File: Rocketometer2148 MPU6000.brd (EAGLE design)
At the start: 55.9 x 22.9 mm, 70 parts, among them J001 USB_MICROB_JST, J301 JST 2mm, J401 M06, J402 M06, J701 MICROSD-SOCKET, Q050 PMOS, U101 BMP180, U201 5319, U301 73831, U401 LPC2148, U601 MPU6000, U801 HMC5883L, U902 ADXL377, Y401 12MHz, Y402 32kiHz

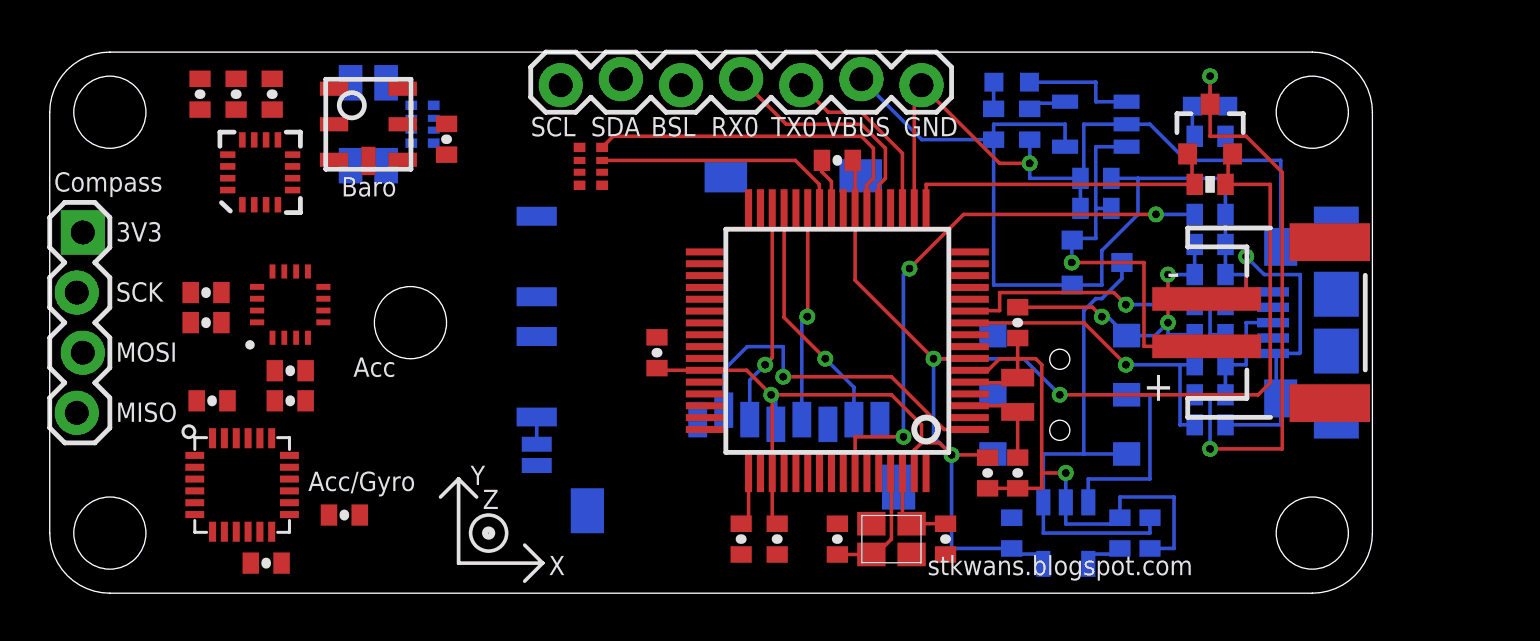
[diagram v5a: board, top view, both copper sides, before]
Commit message: Finished routing shorter board
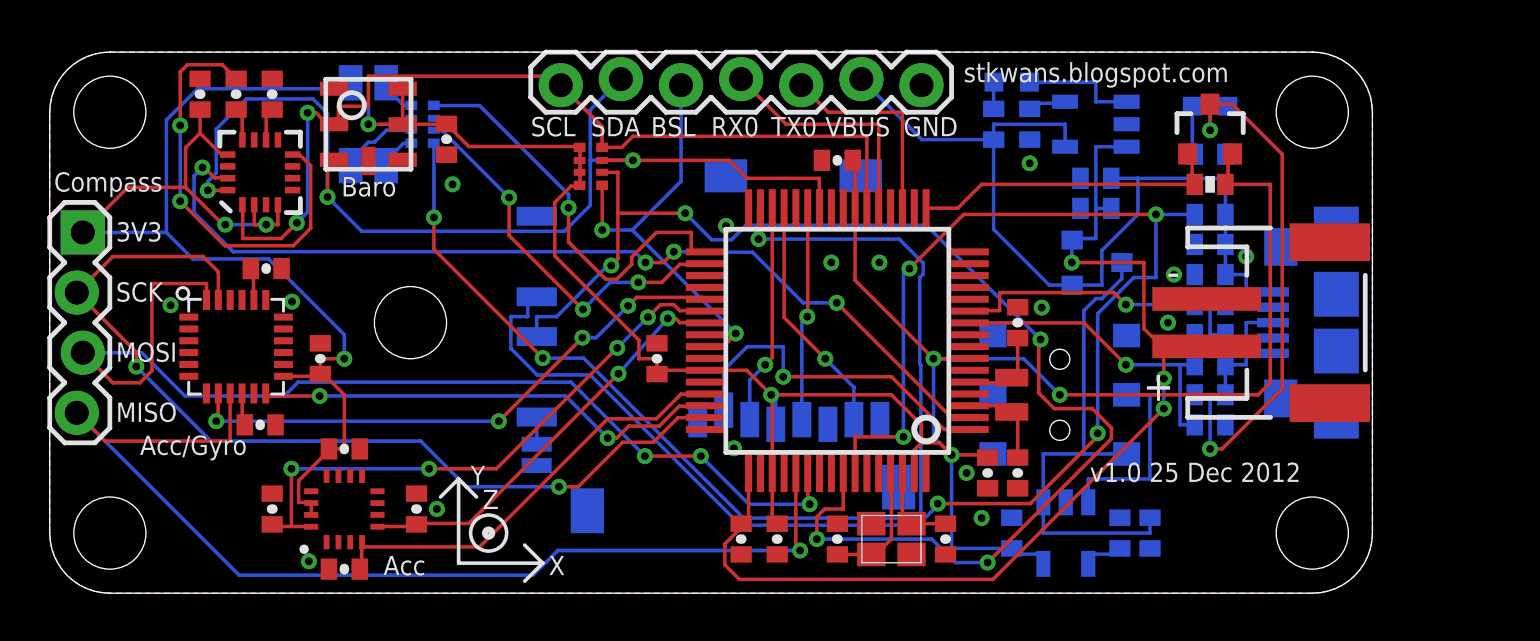
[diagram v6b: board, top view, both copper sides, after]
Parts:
- moved U902 8.93 mm to (12.4, 3.56)
- moved C914 8.82 mm to (12.4, 6.10), turned to 0 degrees
- moved C904 8.69 mm to (12.4, 1.02)
- moved C916 8.36 mm to (9.40, 3.56), turned to 90 degrees
- moved C905 7.03 mm to (15.5, 3.56), turned to 90 degrees
- moved C613 6.68 mm to (11.4, 9.91), turned to 270 degrees
- moved C620 6.04 mm to (9.14, 13.7), turned to 180 degrees
- moved C610 5.85 mm to (8.89, 7.11)
- moved U601 5.85 mm to (7.87, 10.4)
- moved R050 0.76 mm to (49.0, 18.5)
- moved C443 0.25 mm to (25.7, 9.91)
- moved Y402 0.25 mm to (40.6, 8.38)
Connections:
- net XACC: now also U401.39; no longer U401.38
- net ZACC: now also U401.38; no longer U401.39
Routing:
- net GND: track 88.6 -> 0.00 mm, vias 6 -> 16
- net VCC: track 75.6 -> 157.2 mm, vias 4 -> 8
- net RESET: track 0.00 -> 55.4 mm, vias 0 -> 5
- net PWMR: track 0.00 -> 49.2 mm, vias 0 -> 3
- net MISO1: track 0.00 -> 46.2 mm, vias 0 -> 1
- net MOSI1: track 0.00 -> 45.5 mm, vias 0 -> 3
- net USB_ON: track 23.8 -> 67.5 mm, vias 3 -> 5
- net COMPINT: track 0.00 -> 40.1 mm, vias 0 -> 4
- net SCK1: track 0.00 -> 39.6 mm, vias 0 -> 2
- net SDA0: track 10.6 -> 45.0 mm, vias 0 -> 3
- net VLIPO: track 19.5 -> 47.3 mm, vias 1 -> 3
- net SCL0: track 14.5 -> 39.7 mm, vias 0 -> 2
- net ZACC: track 0.00 -> 24.6 mm, vias 0 -> 4
- net CSA: track 0.00 -> 24.1 mm, vias 0 -> 4
- net ACCINT: track 0.00 -> 19.9 mm, vias 0 -> 2
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- added copper zone on layer 1, net GND
- added copper zone on layer 16, net GND

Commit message: RocketometerMPU sent to Laen
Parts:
- J401: value M06 -> M07
- J402: value M06 -> M04
- U201: value 5319 -> MIC5319
- U301: value 73831 -> MCP73831
- moved JP4 17.8 mm to (53.3, 2.54)
- moved JP5 17.8 mm to (53.3, 20.3)
- moved U$1 1.52 mm to (8.13, 4.57)
- moved R051 0.25 mm to (49.0, 17.0)
- renumbered C407 to C463
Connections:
- removed net HACCINT: U401.14
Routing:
- net SDA0: track 45.0 -> 43.6 mm
- net PWMG: track 17.5 -> 16.2 mm
- net N$6: track 23.7 -> 23.0 mm
- net PWMB: track 16.3 -> 16.6 mm, vias 3 -> 1
- net XACC: track 17.6 -> 17.4 mm, vias 2 -> 0
- net ZACC: track 24.6 -> 24.4 mm, vias 4 -> 2
- net CSA: track 24.1 -> 24.0 mm, vias 4 -> 2
- net VCC: track 157.2 -> 157.3 mm, vias 8 -> 10
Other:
- board text added: "RocketometerMPU"
- board text added: "v1.0 13 Nov 2012"
- board text removed: "Rocketometer2148"
- board text removed: "v1.0 25 Dec 2012"

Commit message: Packaging for push
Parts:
- added C907: 100nF, SparkFun-Passives:0402-CAP
- added C908: 10uF, SparkFun:0603-CAP
- added U901: ADXL377, KwanSystems:ADXL377
- J401: device SparkFun-Connectors:1X07_LOCK -> SparkFun-Connectors:1X07
- J402: device SparkFun-Connectors:1X04_LOCK -> SparkFun-Connectors:1X04
- U902: value ADXL377 -> AD7995; device KwanSystems:ADXL377 -> KwanSystems:SOT-23-8
- moved U$4 30.5 mm to (47.8, 1.02)
- moved C916 3.56 mm to (5.84, 3.56)
- moved C904 3.56 mm to (8.89, 1.02)
- moved C905 3.56 mm to (11.9, 3.56)
- moved C914 3.56 mm to (8.89, 6.10)
- moved U902 3.05 mm to (15.5, 3.56), turned to 0 degrees
- moved C405 0.51 mm to (40.9, 10.9)
- moved C620 0.25 mm to (9.14, 14.0)
- moved C610 0.25 mm to (8.89, 7.37)
- moved C613 0.25 mm to (11.4, 10.2)
- moved U601 0.25 mm to (7.87, 10.7)
- moved Y402 0.25 mm to (40.9, 8.38)
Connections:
- net GND: now also C907.2, C908.2, J401.2, U901.2, U901.6, U901.7; no longer J401.1, U902.2, U902.6
- net SCL0: now also U902.1
- net SDA0: now also U902.2
- net VBUS: now also J401.1; no longer J401.2
- net VCC: now also C907.1, C908.1, U901.14, U901.15, U902.8; no longer U902.14, U902.15
- net XACC: now also U901.5, U902.3; no longer U401.39, U902.5
- net YACC: now also U901.4; no longer U401.45
- net ZACC: now also U901.16, U902.6; no longer U401.38, U902.16
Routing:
- net PWMR: track 49.1 -> 15.6 mm, vias 3 -> 1
- net RESET: track 55.0 -> 23.9 mm, vias 5 -> 2
- net USB_ON: track 67.5 -> 41.7 mm, vias 5 -> 3
- net SDA0: track 43.6 -> 66.1 mm, vias 3 -> 9
- net SCL0: track 39.7 -> 60.8 mm, vias 2 -> 7
- net VCC: track 157.3 -> 173.3 mm, vias 10 -> 9
- net CSA: track 24.0 -> 37.3 mm
- net MISO1: track 46.2 -> 58.7 mm, vias 1 -> 4
- net COMPINT: track 40.4 -> 52.9 mm, vias 4 -> 6
- net VBUS: track 37.4 -> 49.6 mm
- net N$14: track 18.4 -> 6.81 mm, vias 2 -> 0
- net XACC: track 17.4 -> 6.78 mm
- net ZACC: track 24.4 -> 14.5 mm
- net YACC: track 18.5 -> 8.88 mm
- net PWMB: track 16.6 -> 24.9 mm, vias 1 -> 3
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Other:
- board text added: "HighAcc"
- board text added: "v1.1 13 Nov 2012"
- board text removed: "Acc"
- board text removed: "v1.0 13 Nov 2012"
